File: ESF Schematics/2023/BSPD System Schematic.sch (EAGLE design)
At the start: 44 parts, among them Q1 MOSFET_N-CHANNEL, Q2 MOSFET_P-CHANNEL, U1 OPAMP, U10 LOGICGATE_NOR, U2 OPAMP, U3 OPAMP, U4 OPAMP, U5 OPAMP, U6 OPAMP, U7 OPAMP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

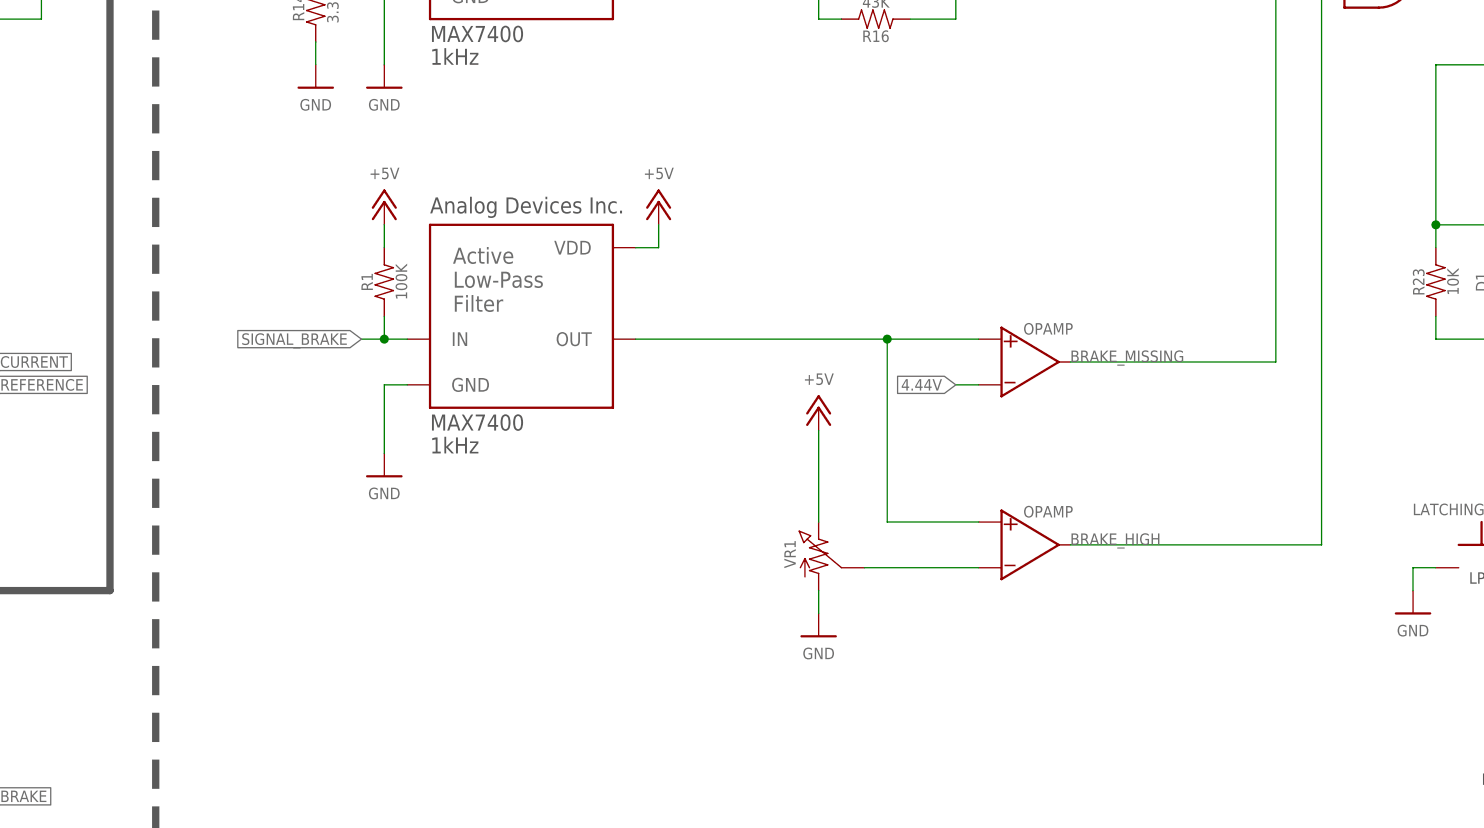
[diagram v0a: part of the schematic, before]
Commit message: added non-specced bse switch
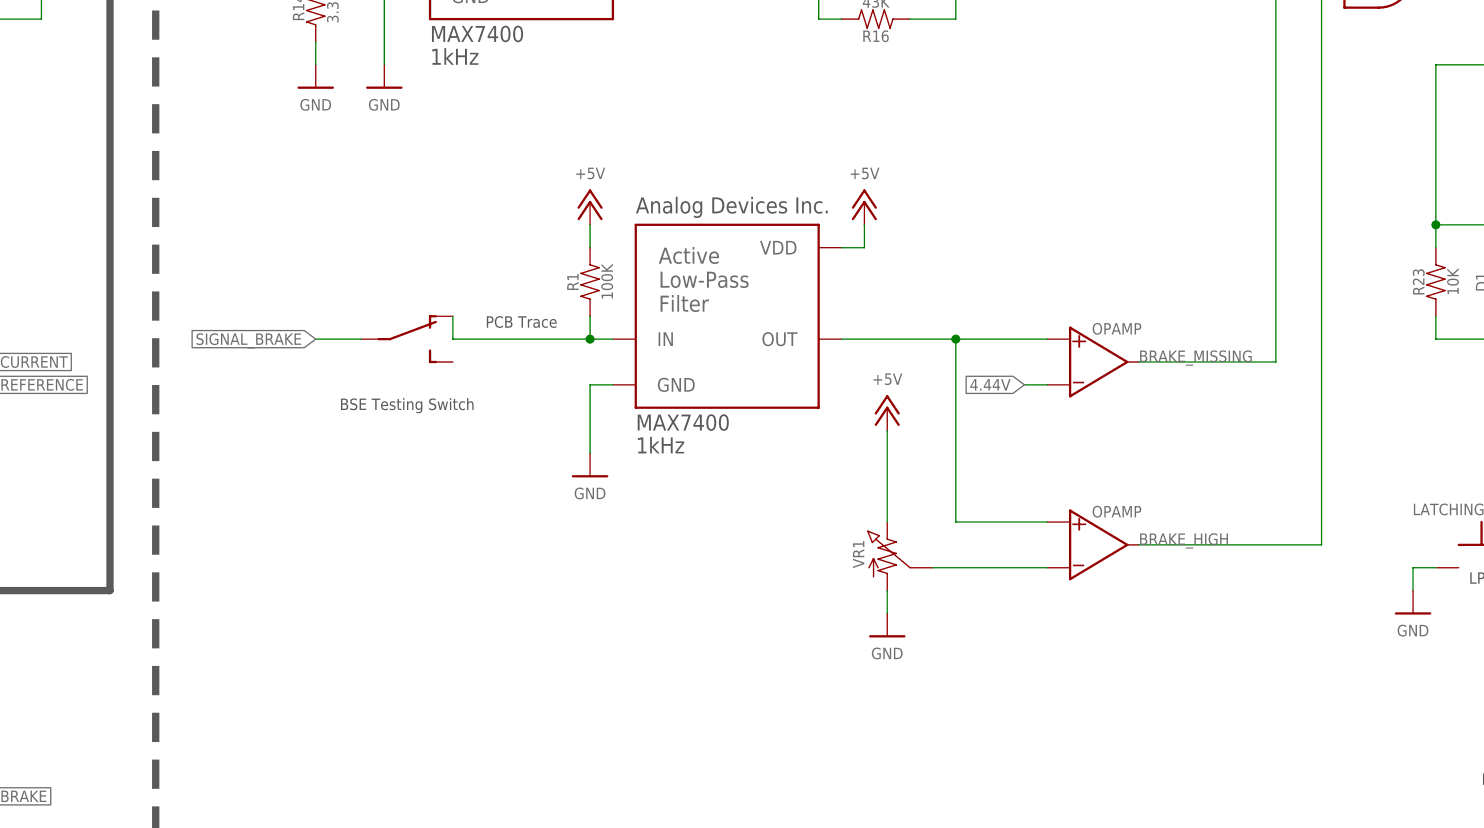
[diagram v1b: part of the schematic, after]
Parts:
- added S1: SWITCH_SPST_, HyTechSymbols:SWITCH_SPST_
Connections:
- net SIGNAL_BRAKE: now also S1.O, S1.P
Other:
- note added: "BSE Testing Switch"
- moved on the sheet: R1, VR1

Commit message: minor changes, still cursed
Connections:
- net 4.44V renamed 4.45V
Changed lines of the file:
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@@
 </segment>
 </net>
-<net name="4.44V" class="0">
+<net name="4.45V" class="0">
 <segment>
 <pinref part="U7" gate="G$1" pin="VIN-"/>

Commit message: after review
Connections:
- removed net SHUTDOWN_C: BSPD_RELAY.6
- new net SHUTDOWN_E: BSPD_RELAY.5
- net SHUTDOWN_D: now also BSPD_RELAY.6; no longer BSPD_RELAY.5
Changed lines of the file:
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@@
 </segment>
 </net>
-<net name="SHUTDOWN_C" class="0">
+<net name="N$5" class="0">
+<segment>
+<wire x1="33.02" y1="15.24" x2="43.18" y2="15.24" width="0.0762" layer="91"/>
+</segment>
+</net>
+<net name="SHUTDOWN_D" class="0">
 <segment>
 <pinref part="BSPD_RELAY" gate="G$1" pin="6"/>
 <wire x1="236.22" y1="58.42" x2="233.68" y2="58.42" width="0.0762" layer="91"/>
 <label x="233.68" y="58.42" size="1.27" layer="95" rot="R180" xref="yes"/>
-</segment>
-</net>
-<net name="N$5" class="0">
-<segment>
-<wire x1="33.02" y1="15.24" x2="43.18" y2="15.24" width="0.0762" layer="91"/>
-</segment>
-</net>
-<net name="SHUTDOWN_D" class="0">
-<segment>
-<pinref part="BSPD_RELAY" gate="G$1" pin="5"/>
-<wire x1="251.46" y1="60.96" x2="254" y2="60.96" width="0.0762" layer="91"/>
-<label x="254" y="60.96" size="1.27" layer="95" xref="yes"/>
 </segment>
 </net>
@@
 </segment>
 </net>
+<net name="SHUTDOWN_E" class="0">
+<segment>
+<pinref part="BSPD_RELAY" gate="G$1" pin="5"/>
+<wire x1="251.46" y1="60.96" x2="254" y2="60.96" width="0.0762" layer="91"/>
+<label x="254" y="60.96" size="1.27" layer="95" xref="yes"/>
+</segment>
+</net>

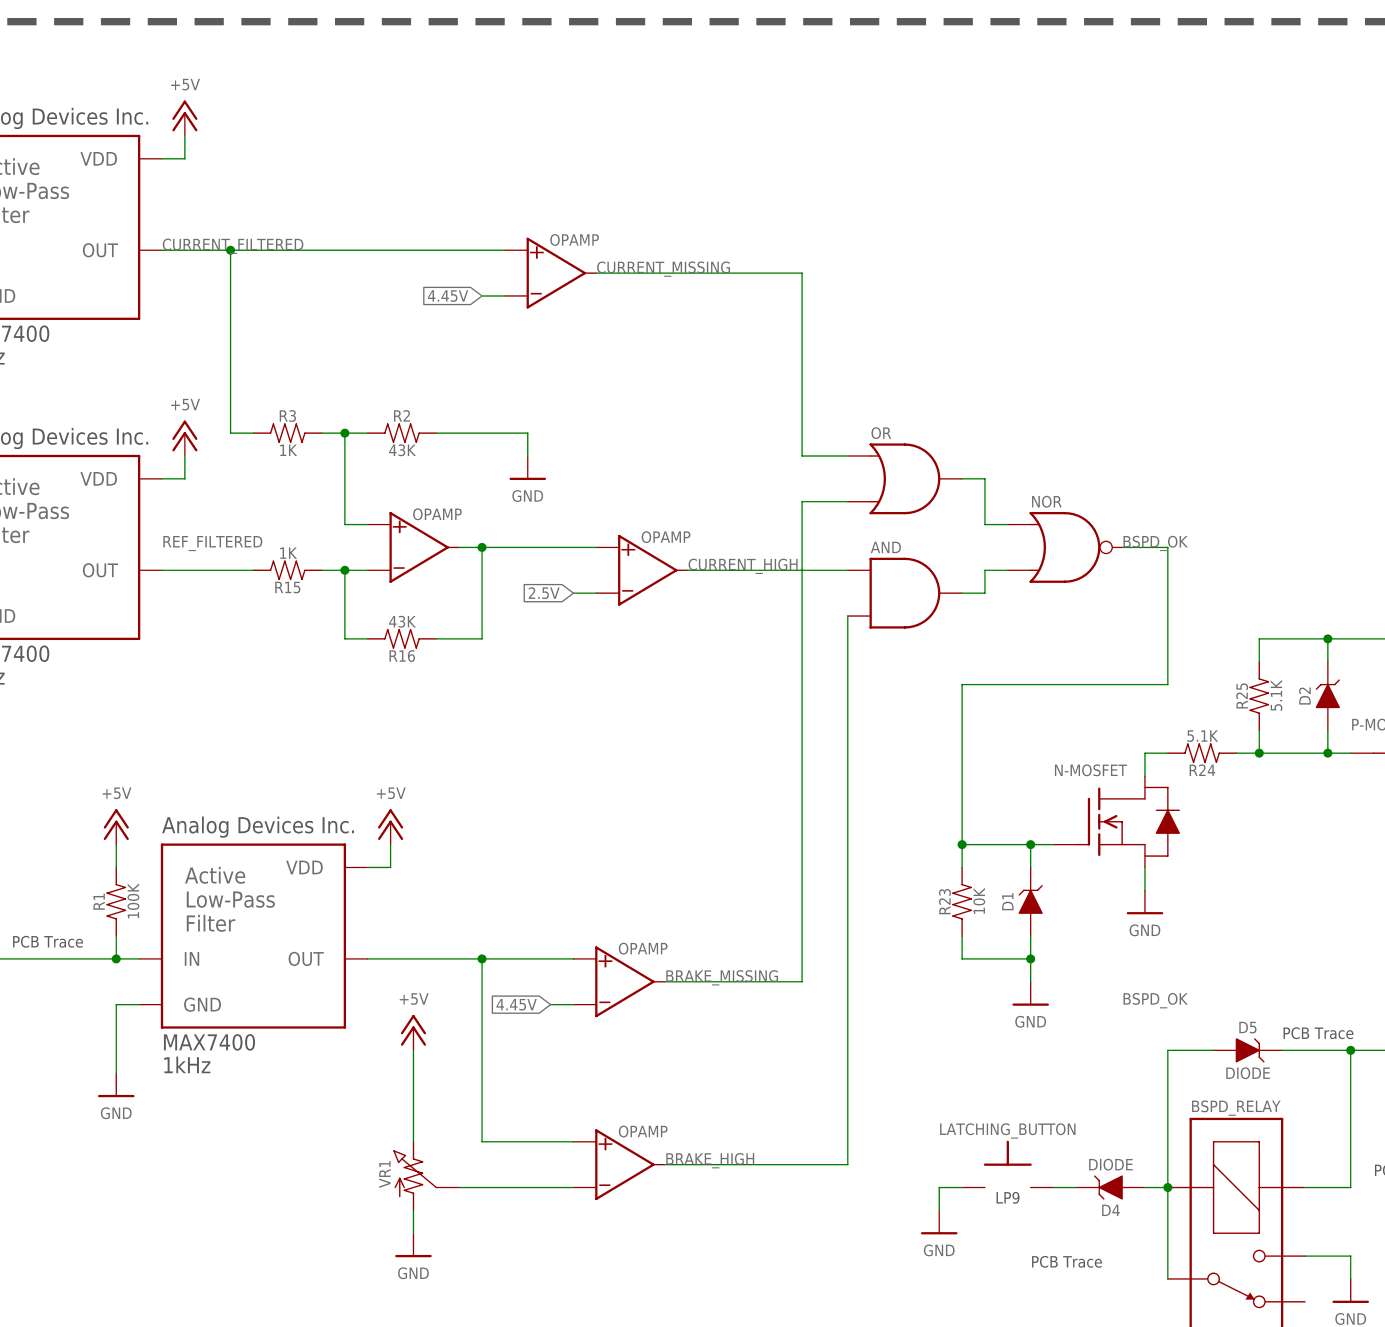
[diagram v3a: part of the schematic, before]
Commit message: changed BSPD, fixed precharger vdd
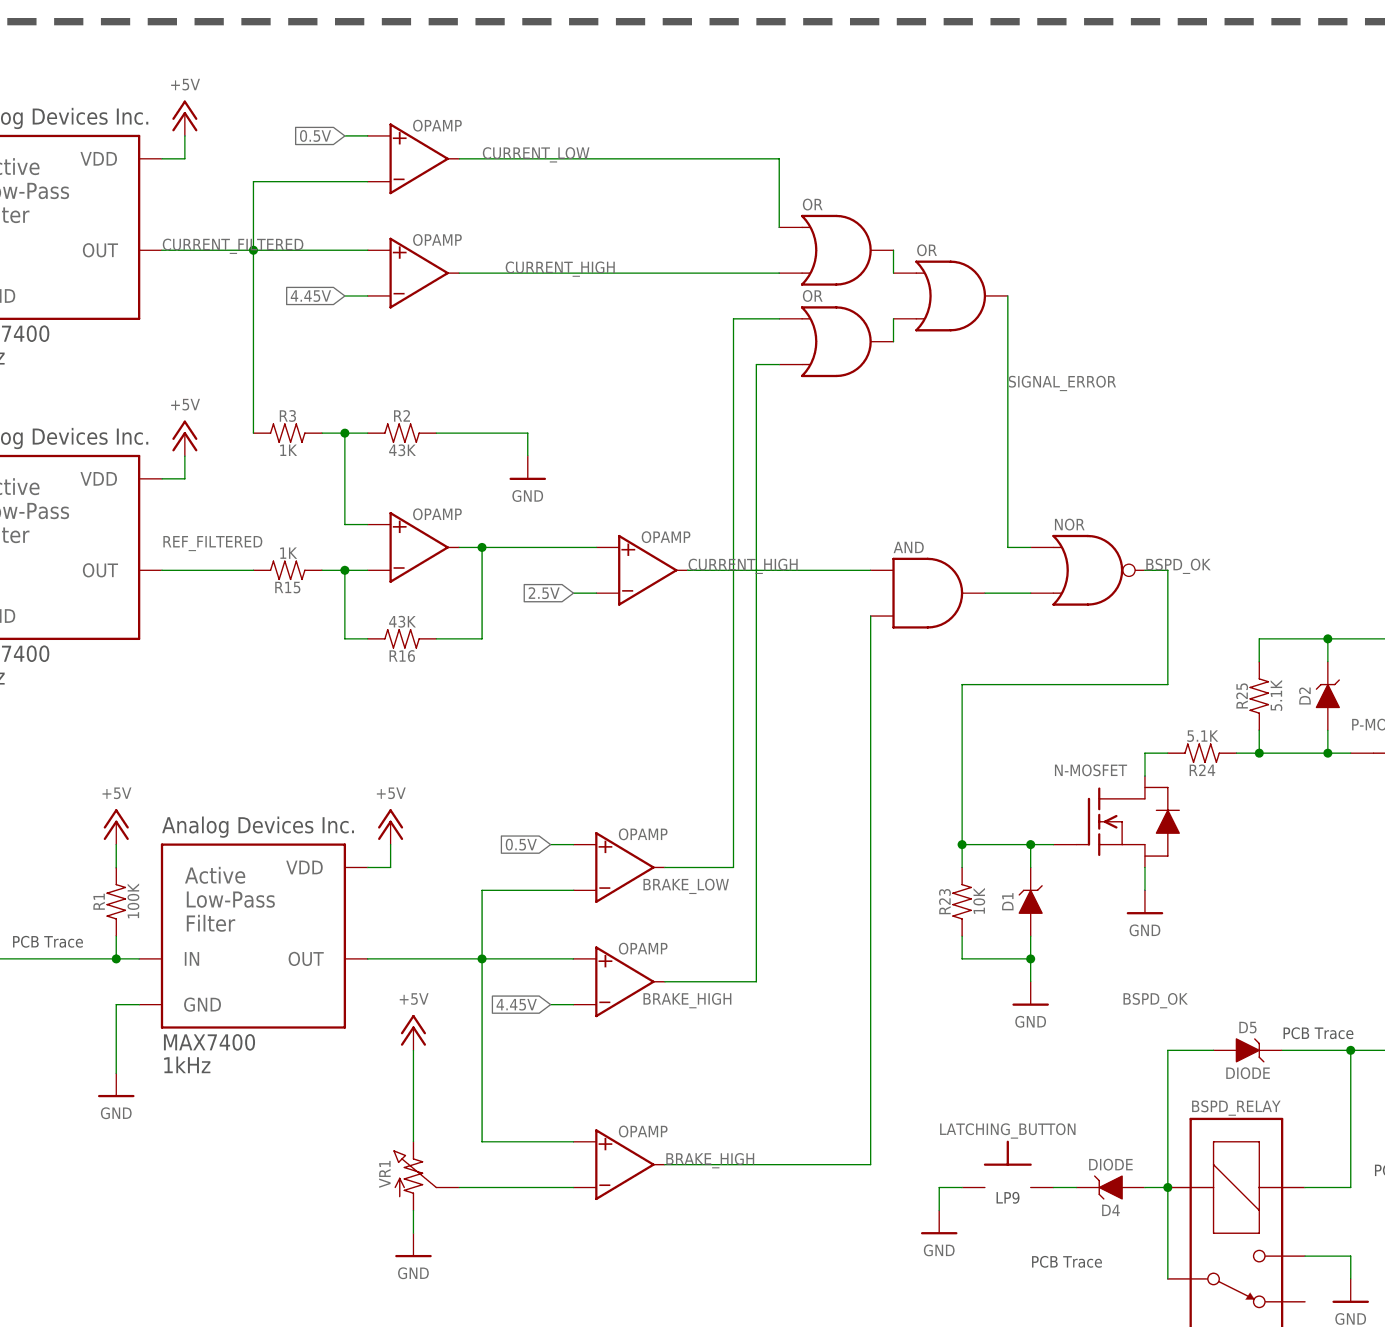
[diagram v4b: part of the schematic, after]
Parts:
- added U11, U14: OPAMP, HyTechSymbols:OPAMP
- added U12, U13: LOGICGATE_OR, HyTechSymbols:LOGICGATE_OR
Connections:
- net N$9 renamed SIGNAL_ERROR
- removed net BRAKE_MISSING: U1.VOUT, U8.IN2
- removed net CURRENT_MISSING: U7.VOUT, U8.IN1
- new net 0.5V: U11.VIN+, U14.VIN+
- new net BRAKE_LOW: U11.VOUT, U13.IN1
- new net CURRENT_LOW: U12.IN1, U14.VOUT
- new net N$15: U12.OUT, U8.IN1
- new net N$18: U13.OUT, U8.IN2
- net BRAKE_HIGH: now also U1.VOUT, U13.IN2
- net CURRENT_FILTERED: now also U14.VIN-
- net CURRENT_HIGH: now also U12.IN2, U7.VOUT
- net SIGNAL_BRAKE: now also U11.VIN-

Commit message: removed pull ups on BSPD inputs
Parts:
- removed R19: 100k, HyTechSymbols:RESISTOR
- removed R20: 100K, HyTechSymbols:RESISTOR
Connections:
- net +24V: no longer R19.2, R20.2
- net CURRENT_BOOSTED: no longer R19.1
- net REFERENCE_BOOSTED: no longer R20.1
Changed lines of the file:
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@@
 <part name="U6" library="HyTechSymbols" deviceset="OPAMP" device=""/>
 <part name="U7" library="HyTechSymbols" deviceset="OPAMP" device=""/>
-<part name="R19" library="HyTechSymbols" deviceset="RESISTOR" device="" value="100k"/>
-<part name="R20" library="HyTechSymbols" deviceset="RESISTOR" device="" value="100K"/>
-<part name="U$3" library="HyTechSupplies" deviceset="+24V" device=""/>
-<part name="U$4" library="HyTechSupplies" deviceset="+24V" device=""/>
 <part name="U$6" library="HyTechSymbols" deviceset="FILTER_ACTIVE" device="" technology="1KHZ"/>
 <part name="P3" library="HyTechSupplies" deviceset="GND" device=""/>
@@
 <instance part="U6" gate="G$1" x="175.26" y="147.32" smashed="yes"/>
 <instance part="U7" gate="G$1" x="149.86" y="180.34" smashed="yes"/>
-<instance part="R19" gate="G$1" x="76.2" y="190.5" smashed="yes" rot="R90">
-<attribute name="NAME" x="74.93" y="189.23" size="1.27" layer="95" rot="R90" align="bottom-center"/>
-<attribute name="VALUE" x="77.47" y="189.23" size="1.27" layer="96" rot="R90" align="top-center"/>
-</instance>
-<instance part="R20" gate="G$1" x="76.2" y="154.94" smashed="yes" rot="R90">
-<attribute name="NAME" x="74.93" y="153.67" size="1.27" layer="95" rot="R90" align="bottom-center"/>
-<attribute name="VALUE" x="77.47" y="153.67" size="1.27" layer="96" rot="R90" align="top-center"/>
-</instance>
-<instance part="U$3" gate="G$1" x="76.2" y="198.12" smashed="yes">
-<attribute name="VALUE" x="76.2" y="203.2" size="1.778" layer="96" align="bottom-center"/>
-</instance>
-<instance part="U$4" gate="G$1" x="76.2" y="162.56" smashed="yes">
-<attribute name="VALUE" x="76.2" y="167.64" size="1.778" layer="96" align="bottom-center"/>
-</instance>
 <instance part="U$6" gate="G$1" x="124.46" y="116.84" smashed="yes">
 <attribute name="MANUFACTURER" x="124.46" y="118.11" size="1.778" layer="97"/>
@@
 <pinref part="R10" gate="G$1" pin="2"/>
 <label x="55.88" y="182.88" size="1.27" layer="95"/>
-<pinref part="R19" gate="G$1" pin="1"/>
 <wire x1="76.2" y1="182.88" x2="58.42" y2="182.88" width="0.2286" layer="91"/>
-<wire x1="76.2" y1="185.42" x2="76.2" y2="182.88" width="0.0762" layer="91"/>
-<junction x="76.2" y="182.88"/>
 </segment>
 </net>
@@
 <pinref part="R12" gate="G$1" pin="2"/>
 <label x="55.88" y="147.32" size="1.27" layer="95"/>
-<pinref part="R20" gate="G$1" pin="1"/>
 <wire x1="76.2" y1="147.32" x2="78.74" y2="147.32" width="0.0762" layer="91"/>
-<wire x1="76.2" y1="149.86" x2="76.2" y2="147.32" width="0.0762" layer="91"/>
-<junction x="76.2" y="147.32"/>
 </segment>
 </net>
@@
 <net name="+24V" class="0">
 <segment>
-<pinref part="U$4" gate="G$1" pin="+24V"/>
-<pinref part="R20" gate="G$1" pin="2"/>
-<wire x1="76.2" y1="160.02" x2="76.2" y2="157.48" width="0.0762" layer="91"/>
-</segment>
-<segment>
-<pinref part="U$3" gate="G$1" pin="+24V"/>
-<pinref part="R19" gate="G$1" pin="2"/>
-<wire x1="76.2" y1="195.58" x2="76.2" y2="193.04" width="0.0762" layer="91"/>
-</segment>
-<segment>
 <pinref part="Q2" gate="G$1" pin="S"/>

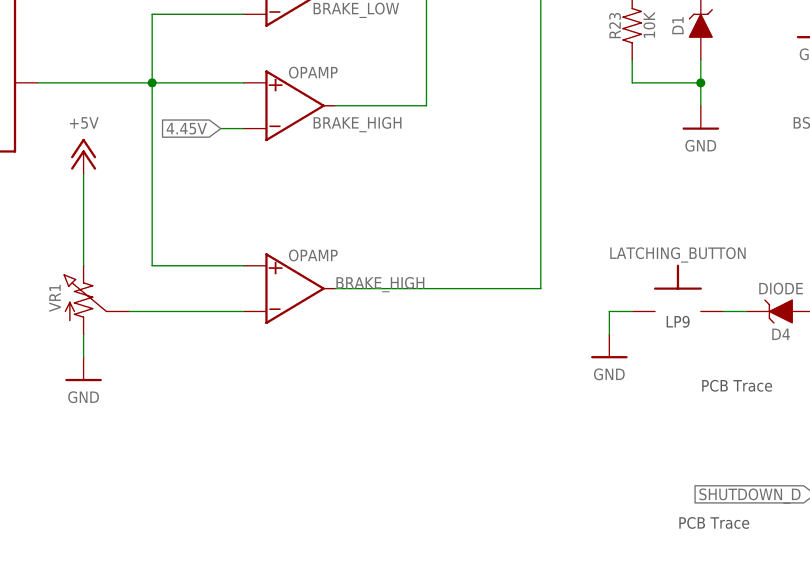
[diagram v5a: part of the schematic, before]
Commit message: finalized schematics for rev2, pics added
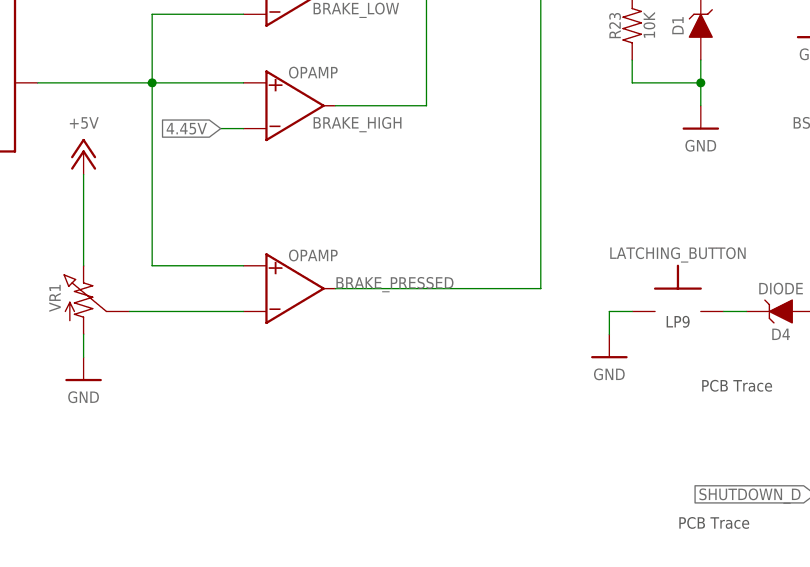
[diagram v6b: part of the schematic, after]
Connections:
- new net BRAKE_PRESSED: U2.VOUT, U9.IN2
- net BRAKE_HIGH: no longer U2.VOUT, U9.IN2
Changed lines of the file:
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@@
 <net name="BRAKE_HIGH" class="0">
-<segment>
-<pinref part="U2" gate="G$1" pin="VOUT"/>
-<wire x1="180.34" y1="81.28" x2="203.2" y2="81.28" width="0.0762" layer="91"/>
-<label x="180.34" y="81.28" size="1.27" layer="95"/>
-<pinref part="U9" gate="G$1" pin="IN2"/>
-<wire x1="203.2" y1="142.24" x2="203.2" y2="81.28" width="0.0762" layer="91"/>
-</segment>
 <segment>
 <pinref part="U1" gate="G$1" pin="VOUT"/>
@@
 </segment>
 </net>
+<net name="BRAKE_PRESSED" class="0">
+<segment>
+<pinref part="U2" gate="G$1" pin="VOUT"/>
+<wire x1="180.34" y1="81.28" x2="203.2" y2="81.28" width="0.0762" layer="91"/>
+<label x="180.34" y="81.28" size="1.27" layer="95"/>
+<pinref part="U9" gate="G$1" pin="IN2"/>
+<wire x1="203.2" y1="142.24" x2="203.2" y2="81.28" width="0.0762" layer="91"/>
+</segment>
+</net>
